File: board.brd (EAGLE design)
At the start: 100 x 80 mm, 32 parts, among them IC1 7805T, J1 350428-1

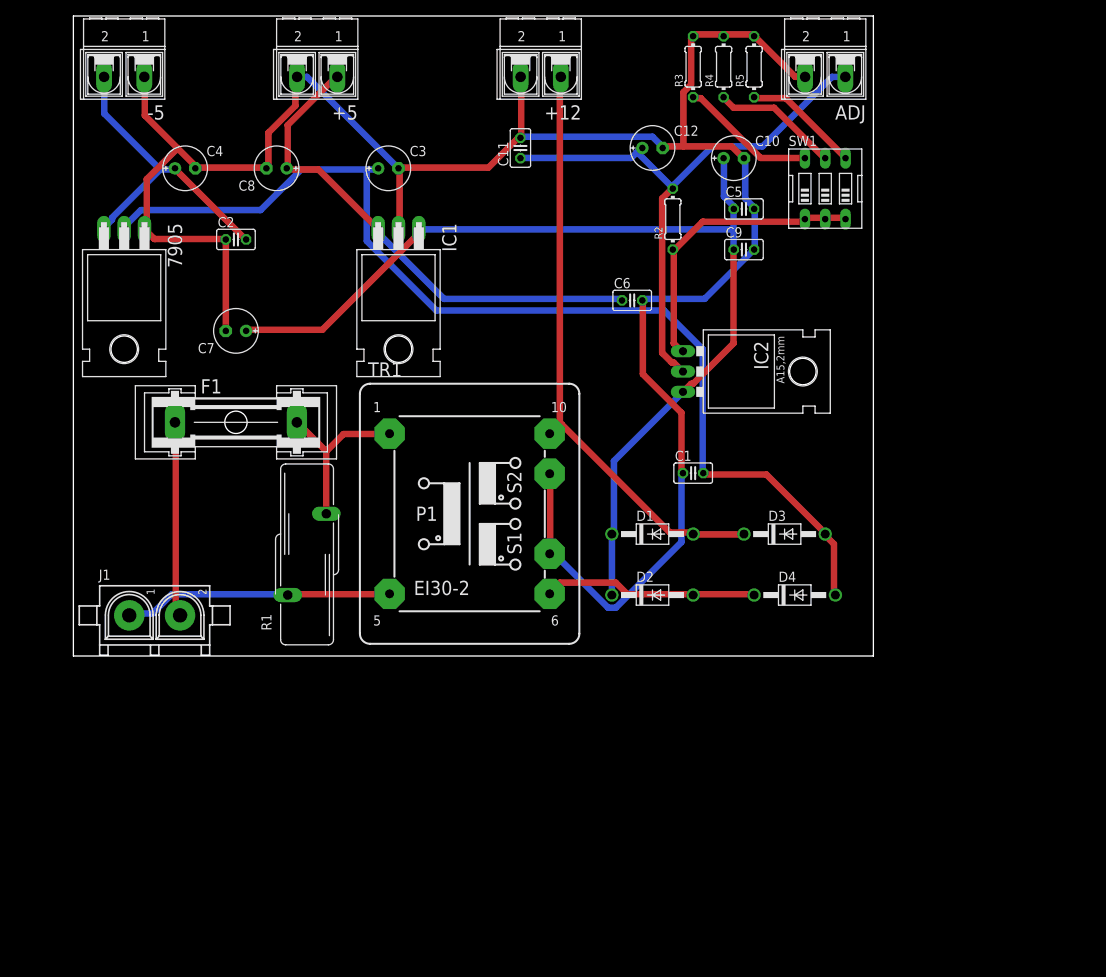
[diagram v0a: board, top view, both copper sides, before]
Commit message: Reposicionando na board
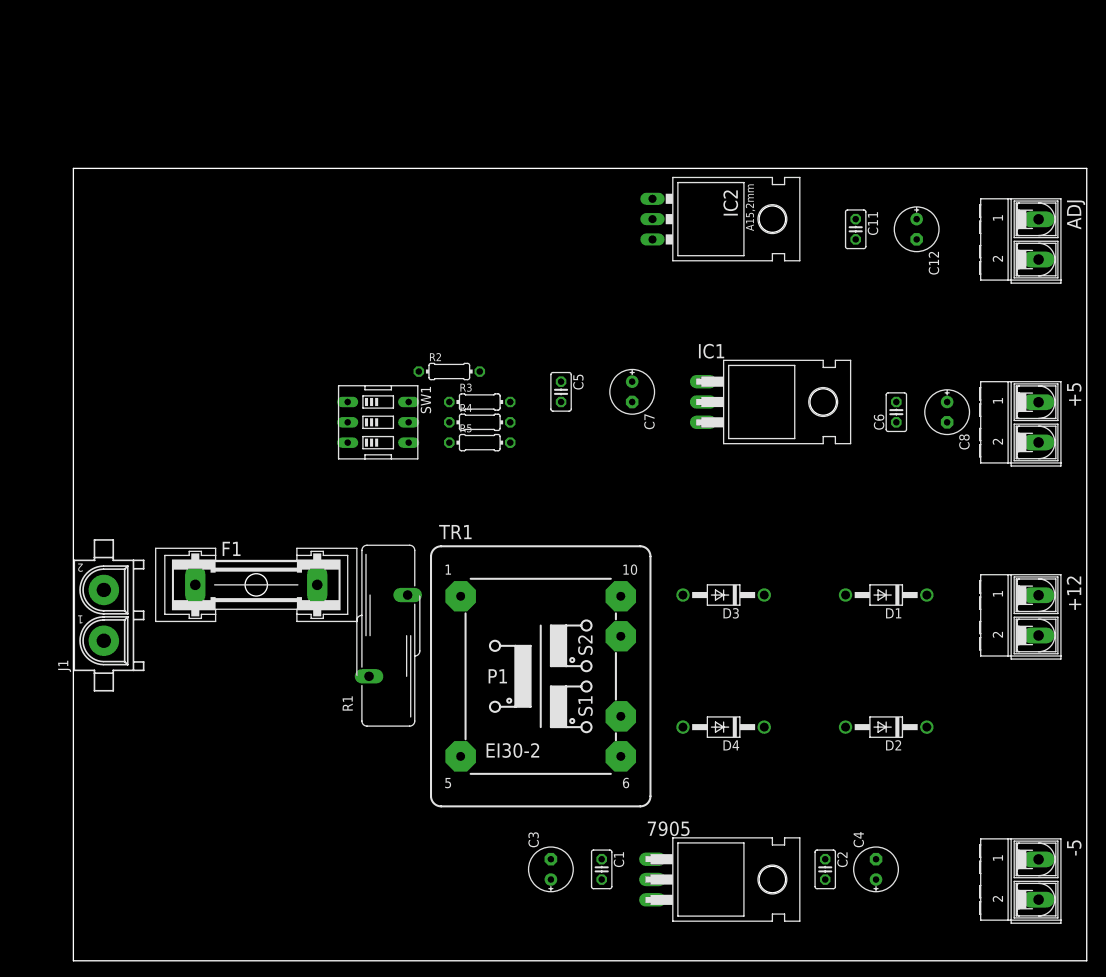
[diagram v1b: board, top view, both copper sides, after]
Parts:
- removed C10: (no value), rcl:E2,5-6E
- removed C9: (no value), rcl:C025-025X050
- moved -5 152.1 mm to (120.7, -27.9), turned to 270 degrees
- moved C4 123.0 mm to (100.3, -26.7), turned to 90 degrees
- moved C2 107.8 mm to (94.0, -26.7), turned to 270 degrees
- moved 7905 104.2 mm to (82.5, -27.9), turned to 270 degrees
- moved +5 100.0 mm to (120.7, 29.2), turned to 270 degrees
- moved +12 91.7 mm to (120.7, 5.08), turned to 270 degrees
- moved C3 90.0 mm to (59.7, -26.7), turned to 90 degrees
- moved C8 89.2 mm to (109.2, 30.5), turned to 270 degrees
- moved SW1 63.1 mm to (38.1, 29.2), turned to 270 degrees
- moved R5 58.2 mm to (50.8, 26.7), turned to 0 degrees
- moved R4 53.9 mm to (50.8, 29.2), turned to 0 degrees
- moved C1 50.8 mm to (66.0, -26.7), turned to 270 degrees
- moved C7 50.1 mm to (69.8, 33.0), turned to 270 degrees
- moved R3 49.7 mm to (50.8, 31.8), turned to 0 degrees
- moved IC1 49.6 mm to (88.9, 31.8), turned to 270 degrees
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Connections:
- net GND: no longer C10.-, C9.2
- net N$10: no longer C10.+, C9.1
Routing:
- net GND: track 273.8 -> 0.00 mm
- net N$6: track 133.8 -> 0.00 mm
- net N$10: track 128.2 -> 0.00 mm
- net N$4: track 75.6 -> 0.00 mm
- net N$11: track 74.4 -> 0.00 mm
- net N$9: track 63.2 -> 0.00 mm
- net N$8: track 39.4 -> 0.00 mm
- net N$13: track 36.9 -> 0.00 mm
- net N$2: track 33.9 -> 0.00 mm
- net N$12: track 26.9 -> 0.00 mm
- net N$1: track 24.4 -> 0.00 mm
- net N$3: track 21.8 -> 0.00 mm
- net N$5: track 17.1 -> 0.00 mm
- net N$7: track 15.9 -> 0.00 mm
- net N$14: track 14.6 -> 0.00 mm
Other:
- board size 100 x 80 mm -> 126.7 x 99.1 mm

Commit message: Ajustes na board
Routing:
- net GND: track 0.00 -> 268.1 mm
- net N$10: track 0.00 -> 92.1 mm
- net N$11: track 0.00 -> 81.6 mm
- net N$4: track 0.00 -> 54.5 mm
- net N$13: track 0.00 -> 53.7 mm
- net N$8: track 0.00 -> 50.8 mm
- net N$2: track 0.00 -> 50.6 mm
- net N$6: track 0.00 -> 50.0 mm
- net N$9: track 0.00 -> 43.4 mm
- net N$12: track 0.00 -> 29.6 mm
- net N$3: track 0.00 -> 18.5 mm
- net N$1: track 0.00 -> 11.7 mm
- net N$7: track 0.00 -> 5.08 mm
- net N$5: track 0.00 -> 5.08 mm
- net N$14: track 0.00 -> 5.08 mm
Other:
- board size 126.7 x 99.1 mm -> 130.5 x 99.1 mm

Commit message: Malha de GND e impressões.
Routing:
- net GND: track 268.1 -> 3.56 mm
- added copper zone on layer 16, net GND
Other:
- board text added: "BS-BC-MC-2020"
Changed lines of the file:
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@@
 <layer number="25" name="tNames" color="7" fill="1" visible="yes" active="yes"/>
 <layer number="26" name="bNames" color="7" fill="1" visible="yes" active="yes"/>
-<layer number="27" name="tValues" color="7" fill="1" visible="yes" active="yes"/>
-<layer number="28" name="bValues" color="7" fill="1" visible="yes" active="yes"/>
+<layer number="27" name="tValues" color="7" fill="1" visible="no" active="yes"/>
+<layer number="28" name="bValues" color="7" fill="1" visible="no" active="yes"/>
 <layer number="29" name="tStop" color="7" fill="3" visible="no" active="yes"/>
 <layer number="30" name="bStop" color="7" fill="6" visible="no" active="yes"/>
@@
 <layer number="41" name="tRestrict" color="4" fill="10" visible="yes" active="yes"/>
 <layer number="42" name="bRestrict" color="1" fill="10" visible="yes" active="yes"/>
-<layer number="43" name="vRestrict" color="2" fill="10" visible="yes" active="yes"/>
+<layer number="43" name="vRestrict" color="2" fill="10" visible="no" active="yes"/>
 <layer number="44" name="Drills" color="7" fill="1" visible="no" active="yes"/>
 <layer number="45" name="Holes" color="7" fill="1" visible="no" active="yes"/>
 <layer number="46" name="Milling" color="3" fill="1" visible="no" active="yes"/>
 <layer number="47" name="Measures" color="7" fill="1" visible="no" active="yes"/>
-<layer number="48" name="Document" color="7" fill="1" visible="yes" active="yes"/>
-<layer number="49" name="Reference" color="7" fill="1" visible="yes" active="yes"/>
+<layer number="48" name="Document" color="7" fill="1" visible="no" active="yes"/>
+<layer number="49" name="Reference" color="7" fill="1" visible="no" active="yes"/>
 <layer number="51" name="tDocu" color="7" fill="1" visible="yes" active="yes"/>
 <layer number="52" name="bDocu" color="7" fill="1" visible="yes" active="yes"/>
@@
 <wire x1="126.67" y1="60.95" x2="-3.81" y2="60.95" width="0" layer="20"/>
 <wire x1="-3.81" y1="60.95" x2="-3.81" y2="-38.1" width="0" layer="20"/>
+<text x="16.51" y="-36.83" size="1.778" layer="16" rot="MR0">BS-BC-MC-2020</text>
+<text x="-1.27" y="57.15" size="1.778" layer="1">BS-BC-MC-2020</text>
 </plain>
 <attributes>
@@
 <contactref element="R4" pad="2"/>
 <contactref element="R5" pad="2"/>
-<wire x1="68.4276" y1="2.4638" x2="68.4276" y2="-7.5438" width="0.8128" layer="16"/>
-<wire x1="68.4276" y1="-7.5438" x2="59.69" y2="-16.2814" width="0.8128" layer="16"/>
-<wire x1="59.69" y1="-16.2814" x2="59.69" y2="-25.4" width="0.8128" layer="16"/>
-<wire x1="120.65" y1="2.5654" x2="120.65" y2="-25.4" width="0.8128" layer="16"/>
-<wire x1="120.65" y1="-25.4" x2="100.33" y2="-25.4" width="0.8128" layer="16"/>
-<wire x1="100.33" y1="-25.4" x2="93.98" y2="-25.4" width="0.8128" layer="16"/>
-<wire x1="93.98" y1="-25.4" x2="89.18245" y2="-25.4" width="0.8128" layer="16"/>
-<wire x1="89.18245" y1="-25.4" x2="88.64905" y2="-24.8666" width="0.8128" layer="16"/>
-<wire x1="88.64905" y1="-24.8666" x2="86.10295" y2="-24.8666" width="0.8128" layer="16"/>
-<wire x1="86.10295" y1="-24.8666" x2="85.56955" y2="-25.4" width="0.8128" layer="16"/>
-<wire x1="85.56955" y1="-25.4" x2="72.39" y2="-25.4" width="0.8128" layer="16"/>
-<wire x1="72.39" y1="-25.4" x2="66.04" y2="-25.4" width="0.8128" layer="16"/>
-<wire x1="66.04" y1="-25.4" x2="59.69" y2="-25.4" width="0.8128" layer="16"/>
-<wire x1="123.19" y1="6.9528125" x2="123.19" y2="8.2363875" width="0.8128" layer="16"/>
-<wire x1="120.65" y1="2.5654" x2="120.65" y2="4.4128125" width="0.8128" layer="16"/>
-<wire x1="120.65" y1="10.7763875" x2="120.65" y2="26.6954" width="0.8128" layer="16"/>
-<wire x1="120.65" y1="4.4128125" x2="123.19" y2="6.9528125" width="0.8128" layer="16"/>
-<wire x1="123.19" y1="8.2363875" x2="120.65" y2="10.7763875" width="0.8128" layer="16"/>
-<wire x1="120.65" y1="26.6954" x2="111.7346" y2="26.6954" width="0.8128" layer="16"/>
-<wire x1="111.7346" y1="26.6954" x2="109.22" y2="29.21" width="0.8128" layer="16"/>
-<wire x1="109.22" y1="29.21" x2="105.41" y2="29.21" width="0.8128" layer="16"/>
-<wire x1="105.41" y1="29.21" x2="102.87" y2="31.75" width="0.8128" layer="16"/>
-<wire x1="102.87" y1="31.75" x2="102.87" y2="49.53" width="0.8128" layer="16"/>
-<wire x1="102.87" y1="49.53" x2="105.41" y2="52.07" width="0.8128" layer="16"/>
-<wire x1="105.41" y1="52.07" x2="118.1354" y2="52.07" width="0.8128" layer="16"/>
 <wire x1="118.1354" y1="52.07" x2="120.65" y2="49.5554" width="0.8128" layer="16"/>
-<wire x1="105.41" y1="52.07" x2="97.79" y2="52.07" width="0.8128" layer="16"/>
-<wire x1="92.45295" y1="34.8234" x2="94.99905" y2="34.8234" width="0.8128" layer="16"/>
-<wire x1="78.74" y1="31.75" x2="89.37955" y2="31.75" width="0.8128" layer="16"/>
-<wire x1="98.07245" y1="31.75" x2="102.87" y2="31.75" width="0.8128" layer="16"/>
-<wire x1="89.37955" y1="31.75" x2="92.45295" y2="34.8234" width="0.8128" layer="16"/>
-<wire x1="94.99905" y1="34.8234" x2="98.07245" y2="31.75" width="0.8128" layer="16"/>
-<wire x1="78.74" y1="31.75" x2="69.85" y2="31.75" width="0.8128" layer="16"/>
-<wire x1="69.85" y1="31.75" x2="60.96" y2="31.75" width="0.8128" layer="16"/>
-<wire x1="60.96" y1="31.75" x2="54.61" y2="31.75" width="0.8128" layer="16"/>
-<wire x1="54.61" y1="31.75" x2="54.61" y2="29.21" width="0.8128" layer="16"/>
-<wire x1="54.61" y1="29.21" x2="54.61" y2="26.67" width="0.8128" layer="16"/>
-<wire x1="100.33" y1="-25.4" x2="120.65" y2="-25.4254" width="0" layer="19" extent="1-1"/>
+<polygon width="0.0762" layer="16" isolate="0.8128">
+<vertex x="45.72" y="59.69"/>
+<vertex x="45.72" y="19.05"/>
+<vertex x="50.8" y="19.05"/>
+<vertex x="57.15" y="12.7"/>
+<vertex x="57.15" y="-19.05"/>
+<vertex x="45.72" y="-30.48"/>
+<vertex x="45.72" y="-36.83"/>
+<vertex x="124.46" y="-36.83"/>
+<vertex x="125.73" y="-35.56"/>
+<vertex x="125.73" y="59.69"/>
+</polygon>
 </signal>
 <signal name="N$9" class="1">
@@
 <contactref element="C1" pad="2"/>
 <wire x1="76.2" y1="7.62" x2="76.2" y2="-8.89" width="0.8128" layer="1"/>
-<wire x1="59.69" y1="-27.94" x2="72.39" y2="-27.94" width="0.8128" layer="16"/>
+<wire x1="59.69" y1="-27.94" x2="66.04" y2="-27.94" width="0.8128" layer="16"/>
 <wire x1="74.6252" y1="-25.9786625" x2="73.8068625" y2="-26.797" width="0.8128" layer="1"/>
 <wire x1="73.8068625" y1="-26.797" x2="73.533" y2="-26.797" width="0.8128" layer="1"/>
@@
 <wire x1="76.2" y1="-8.89" x2="74.6252" y2="-10.4648" width="0.8128" layer="1"/>
 <wire x1="74.6252" y1="-10.4648" x2="74.6252" y2="-25.9786625" width="0.8128" layer="1"/>
-<wire x1="72.39" y1="-27.94" x2="66.04" y2="-27.94" width="0" layer="19" extent="1-1"/>
+<wire x1="72.39" y1="-27.94" x2="66.04" y2="-27.94" width="0.8128" layer="16"/>
 </signal>
 <signal name="N$5" class="1">
